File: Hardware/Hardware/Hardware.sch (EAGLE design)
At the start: 9 parts, among them J1 1x10 HEADER "A", J2 1x10 HEADER "B", U1 MAX3232

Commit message: Merged the circuit diagrams
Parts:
- added C11: 1uF, rcl:C-EU025-024X044
- added IC1: 74FST3257DR2G, 74FST3257DR2G:74FST3257DR2G
- added J6: 22-27-2051-05, con-molex:22-27-2051-05
- added Q1, Q2: 200mA/40V, SparkFun-DiscreteSemi:TRANS_NPN-2N3904
- added R1, R2: (no value), rcl:R-EU_0207/7
- added R3, R6: 1K, rcl:R-EU_0207/7
- added R4, R5: 4.7K, rcl:R-EU_0207/7
- added U2: L86-M33, L86-M33:L86-M33
- added U4: 74HC4051D,652, 74HC4051D_652:74HC4051D,652
- U1: device SparkFun-IC-Comms:MAX2323TSSOP -> SparkFun-IC-Comms:MAX2323SOIC16
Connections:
- removed net N$9 (its old number): J1.UART_TX, U1.T1IN
- new net +3V3: C5.2, IC1.VCC, J1.3V3, Q1.C, R3.2, U1.VCC, U2.RESET, U2.VCC, U2.V_BCKP, U4.VCC
- new net N$10: IC1.2B2, U2.RXD1
- new net N$11: IC1.1B1, U1.R1OUT
- new net N$17: IC1.2B1, U1.T1IN
- new net N$18: IC1.S, J1.GPIO_I_A2
- new net N$19: IC1.!OE, J1.SPI_CLK
- new net N$20: J6-1.S, U4.Y0
- new net N$22: J6-2.S, U4.Y1
- new net N$23: J6-3.S, U4.Y2
- new net N$24: J6-4.S, U4.Y3
- new net N$25: R2.2, U4.Z
- new net N$3: IC1.1A, J1.UART_RX
- new net N$47: J1.AIN_A1, R1.2, R2.1
- new net N$49: J2.SPI_CS_D/GPIO_I_B3, U4.S0
- new net N$50: J2.SPI_CS_O/GPIO_I_B4, U4.S1
- new net N$51: J2.GPIO_I_B5, U4.S2
- new net N$52: C11.2, R4.1, R5.1
- new net N$53: C11.1, J2.PWM_B1/GPIO_I_B1
- new net N$54: Q2.B, R5.2, R6.1
- new net N$55: Q1.B, R3.1, R4.2
- new net N$57: Q1.E, Q2.C
- net GND: now also IC1.GND, J2.GND, J6-5.S, Q2.E, R1.1, R6.2, U2.GND, U4.GND, U4.VEE, U4.~E
- net N$5: now also IC1.2A, J1.UART_TX; no longer C5.2, J1.3V3, U1.VCC
- net N$8: now also IC1.1B2, U2.TXD1; no longer J1.UART_RX, U1.R1OUT
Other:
- moved on the sheet: C1, C2, C3, C4, C5, J1, J2, J3

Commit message: Merged and tidied up the circuit, did my part of PCB
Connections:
- net N$10: now also IC1.2B1; no longer IC1.2B2
- net N$11: now also IC1.1B2; no longer IC1.1B1
- net N$17: now also IC1.2B2; no longer IC1.2B1
- net N$18: now also J1.SPI_CLK; no longer J1.GPIO_I_A2
- net N$19: now also J1.GPIO_I_A2; no longer J1.SPI_CLK
- net N$20: now also J6-3.S; no longer J6-1.S
- net N$23: now also J6-1.S; no longer J6-3.S
- net N$8: now also IC1.1B1; no longer IC1.1B2
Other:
- moved on the sheet: J6-1, J6-3
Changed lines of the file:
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@@
 <attribute name="VALUE" x="114.046" y="135.89" size="1.778" layer="96" align="center-left"/>
 </instance>
-<instance part="J6" gate="-1" x="142.24" y="93.98" smashed="yes">
-<attribute name="NAME" x="144.78" y="93.218" size="1.524" layer="95"/>
+<instance part="J6" gate="-1" x="142.24" y="88.9" smashed="yes">
+<attribute name="NAME" x="144.78" y="88.138" size="1.524" layer="95"/>
 </instance>
 <instance part="J6" gate="-2" x="142.24" y="91.44" smashed="yes">
 <attribute name="NAME" x="144.78" y="90.678" size="1.524" layer="95"/>
 </instance>
-<instance part="J6" gate="-3" x="142.24" y="88.9" smashed="yes">
-<attribute name="NAME" x="144.78" y="88.138" size="1.524" layer="95"/>
+<instance part="J6" gate="-3" x="142.24" y="93.98" smashed="yes">
+<attribute name="NAME" x="144.78" y="93.218" size="1.524" layer="95"/>
 </instance>
 <instance part="J6" gate="-4" x="142.24" y="86.36" smashed="yes">
@@
 <net name="N$8" class="0">
 <segment>
-<pinref part="IC1" gate="G$1" pin="1B2"/>
-<wire x1="109.22" y1="152.4" x2="106.68" y2="152.4" width="0.1524" layer="91"/>
-<wire x1="106.68" y1="152.4" x2="106.68" y2="165.1" width="0.1524" layer="91"/>
+<wire x1="106.68" y1="154.94" x2="106.68" y2="165.1" width="0.1524" layer="91"/>
 <wire x1="106.68" y1="165.1" x2="152.4" y2="165.1" width="0.1524" layer="91"/>
 <wire x1="152.4" y1="165.1" x2="152.4" y2="147.32" width="0.1524" layer="91"/>
@@
 <pinref part="U2" gate="G$1" pin="TXD1"/>
 <wire x1="208.28" y1="162.56" x2="200.66" y2="162.56" width="0.1524" layer="91"/>
+<pinref part="IC1" gate="G$1" pin="1B1"/>
+<wire x1="109.22" y1="154.94" x2="106.68" y2="154.94" width="0.1524" layer="91"/>
 </segment>
 </net>
@@
 <wire x1="154.94" y1="162.56" x2="154.94" y2="167.64" width="0.1524" layer="91"/>
 <wire x1="154.94" y1="167.64" x2="104.14" y2="167.64" width="0.1524" layer="91"/>
-<wire x1="104.14" y1="167.64" x2="104.14" y2="144.78" width="0.1524" layer="91"/>
-<pinref part="IC1" gate="G$1" pin="2B2"/>
-<wire x1="104.14" y1="144.78" x2="109.22" y2="144.78" width="0.1524" layer="91"/>
+<wire x1="104.14" y1="167.64" x2="104.14" y2="147.32" width="0.1524" layer="91"/>
+<pinref part="IC1" gate="G$1" pin="2B1"/>
+<wire x1="109.22" y1="147.32" x2="104.14" y2="147.32" width="0.1524" layer="91"/>
 </segment>
 </net>
@@
 <pinref part="U1" gate="G$1" pin="R1OUT"/>
 <wire x1="165.1" y1="109.22" x2="96.52" y2="109.22" width="0.1524" layer="91"/>
-<wire x1="96.52" y1="109.22" x2="96.52" y2="154.94" width="0.1524" layer="91"/>
-<pinref part="IC1" gate="G$1" pin="1B1"/>
-<wire x1="96.52" y1="154.94" x2="109.22" y2="154.94" width="0.1524" layer="91"/>
+<wire x1="96.52" y1="109.22" x2="96.52" y2="152.4" width="0.1524" layer="91"/>
+<pinref part="IC1" gate="G$1" pin="1B2"/>
+<wire x1="109.22" y1="152.4" x2="96.52" y2="152.4" width="0.1524" layer="91"/>
 </segment>
 </net>
@@
 <pinref part="U1" gate="G$1" pin="T1IN"/>
 <wire x1="165.1" y1="114.3" x2="101.6" y2="114.3" width="0.1524" layer="91"/>
-<wire x1="101.6" y1="114.3" x2="101.6" y2="147.32" width="0.1524" layer="91"/>
-<pinref part="IC1" gate="G$1" pin="2B1"/>
-<wire x1="101.6" y1="147.32" x2="109.22" y2="147.32" width="0.1524" layer="91"/>
+<wire x1="101.6" y1="114.3" x2="101.6" y2="144.78" width="0.1524" layer="91"/>
+<pinref part="IC1" gate="G$1" pin="2B2"/>
+<wire x1="109.22" y1="144.78" x2="101.6" y2="144.78" width="0.1524" layer="91"/>
 </segment>
 </net>
@@
 <pinref part="IC1" gate="G$1" pin="S"/>
 <wire x1="109.22" y1="157.48" x2="109.22" y2="162.56" width="0.1524" layer="91"/>
-<wire x1="109.22" y1="162.56" x2="147.32" y2="162.56" width="0.1524" layer="91"/>
-<wire x1="147.32" y1="162.56" x2="147.32" y2="132.08" width="0.1524" layer="91"/>
-<pinref part="J1" gate="G$1" pin="GPIO_I_A2"/>
-<wire x1="55.88" y1="132.08" x2="147.32" y2="132.08" width="0.1524" layer="91"/>
+<wire x1="109.22" y1="162.56" x2="142.24" y2="162.56" width="0.1524" layer="91"/>
+<wire x1="142.24" y1="162.56" x2="142.24" y2="134.62" width="0.1524" layer="91"/>
+<wire x1="142.24" y1="134.62" x2="55.88" y2="134.62" width="0.1524" layer="91"/>
+<pinref part="J1" gate="G$1" pin="SPI_CLK"/>
 </segment>
 </net>
@@
 <pinref part="IC1" gate="G$1" pin="!OE"/>
 <wire x1="134.62" y1="154.94" x2="144.78" y2="154.94" width="0.1524" layer="91"/>
-<wire x1="144.78" y1="154.94" x2="144.78" y2="134.62" width="0.1524" layer="91"/>
-<wire x1="144.78" y1="134.62" x2="55.88" y2="134.62" width="0.1524" layer="91"/>
-<pinref part="J1" gate="G$1" pin="SPI_CLK"/>
+<wire x1="144.78" y1="154.94" x2="144.78" y2="132.08" width="0.1524" layer="91"/>
+<pinref part="J1" gate="G$1" pin="GPIO_I_A2"/>
+<wire x1="144.78" y1="132.08" x2="55.88" y2="132.08" width="0.1524" layer="91"/>
 </segment>
 </net>
@@
 </segment>
 </net>
-<net name="N$20" class="0">
-<segment>
-<pinref part="U4" gate="A" pin="Y0"/>
-<pinref part="J6" gate="-1" pin="S"/>
-<wire x1="134.62" y1="93.98" x2="139.7" y2="93.98" width="0.1524" layer="91"/>
-</segment>
-</net>
 <net name="N$22" class="0">
 <segment>
@@
 <pinref part="J6" gate="-2" pin="S"/>
 <wire x1="134.62" y1="91.44" x2="139.7" y2="91.44" width="0.1524" layer="91"/>
-</segment>
-</net>
-<net name="N$23" class="0">
-<segment>
-<pinref part="J6" gate="-3" pin="S"/>
-<pinref part="U4" gate="A" pin="Y2"/>
-<wire x1="139.7" y1="88.9" x2="134.62" y2="88.9" width="0.1524" layer="91"/>
 </segment>
 </net>
@@
 </segment>
 </net>
+<net name="N$20" class="0">
+<segment>
+<pinref part="U4" gate="A" pin="Y0"/>
+<pinref part="J6" gate="-3" pin="S"/>
+<wire x1="139.7" y1="93.98" x2="134.62" y2="93.98" width="0.1524" layer="91"/>
+</segment>
+</net>
+<net name="N$23" class="0">
+<segment>
+<pinref part="U4" gate="A" pin="Y2"/>
+<pinref part="J6" gate="-1" pin="S"/>
+<wire x1="139.7" y1="88.9" x2="134.62" y2="88.9" width="0.1524" layer="91"/>
+</segment>
+</net>

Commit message: Changes in brd
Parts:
- added J4: 22-27-2021-02, con-molex:22-27-2021-02
- R3, R4, R5, R6: device rcl:R-EU_0207/7 -> rcl:R-EU_0207/2V
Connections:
- net N$53: now also J4-1.S
- net N$57: now also J4-2.S

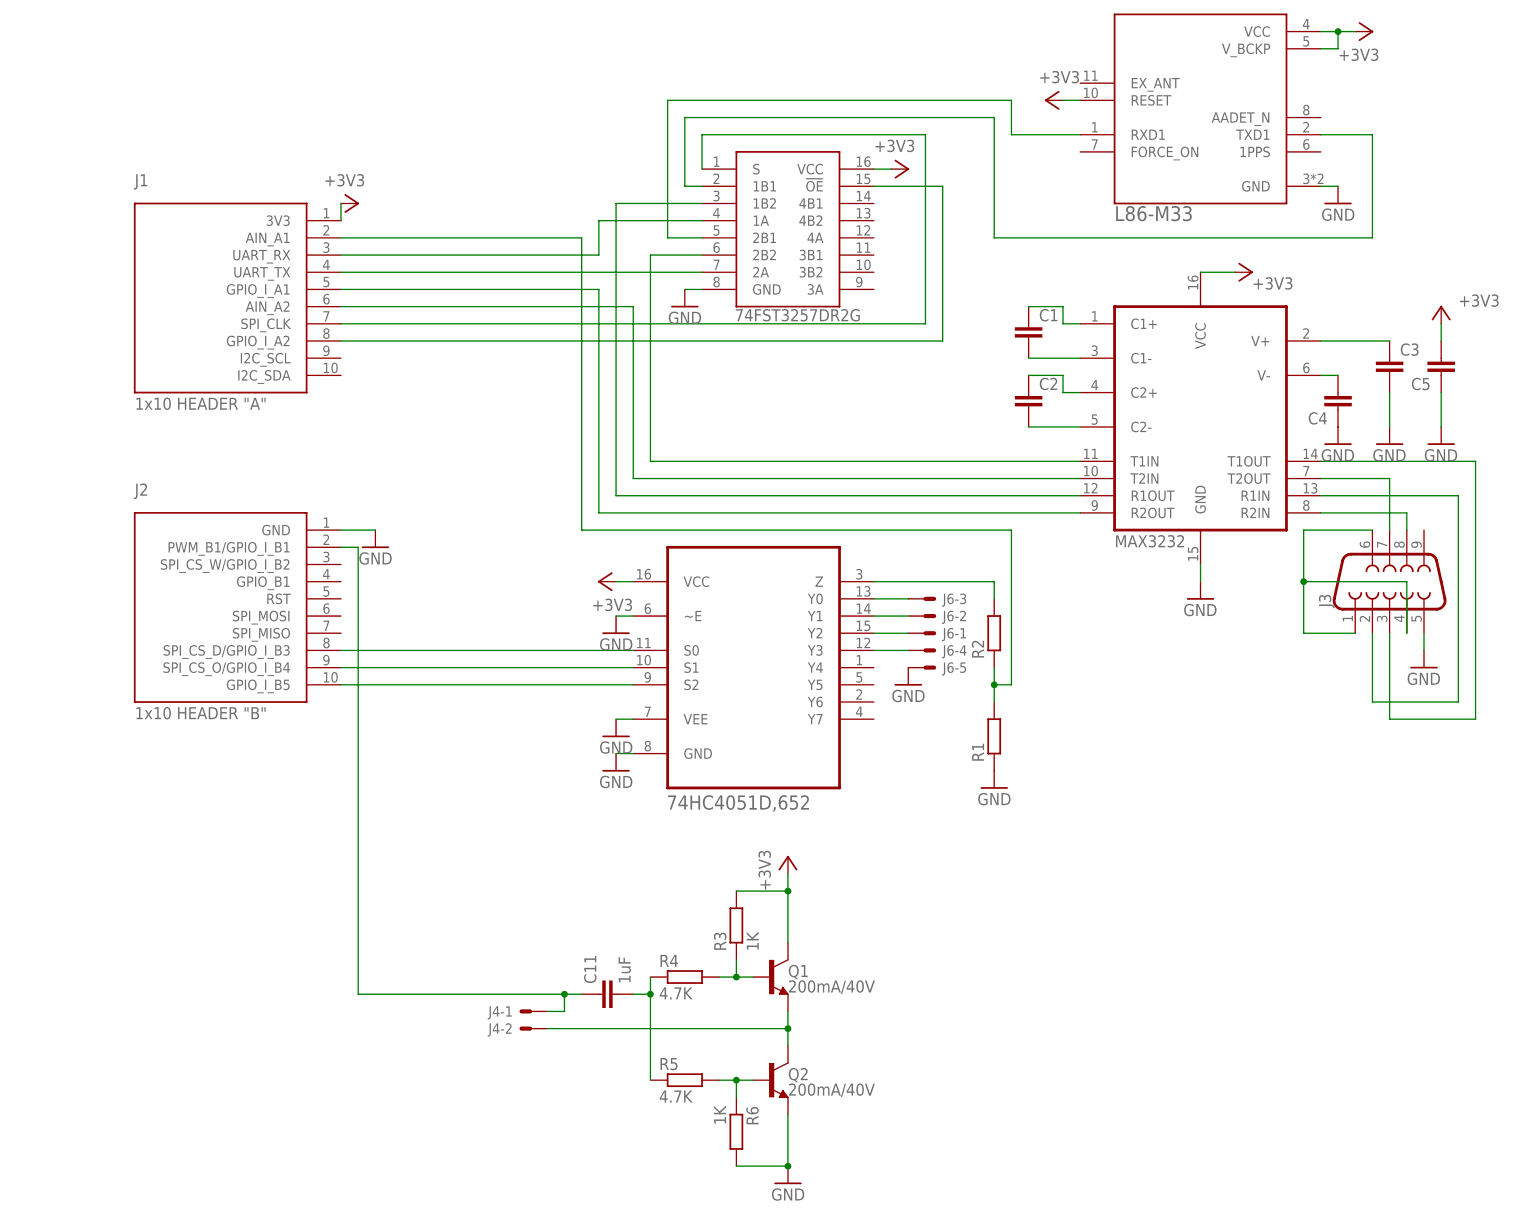
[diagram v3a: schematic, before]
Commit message: Added UART MUX support
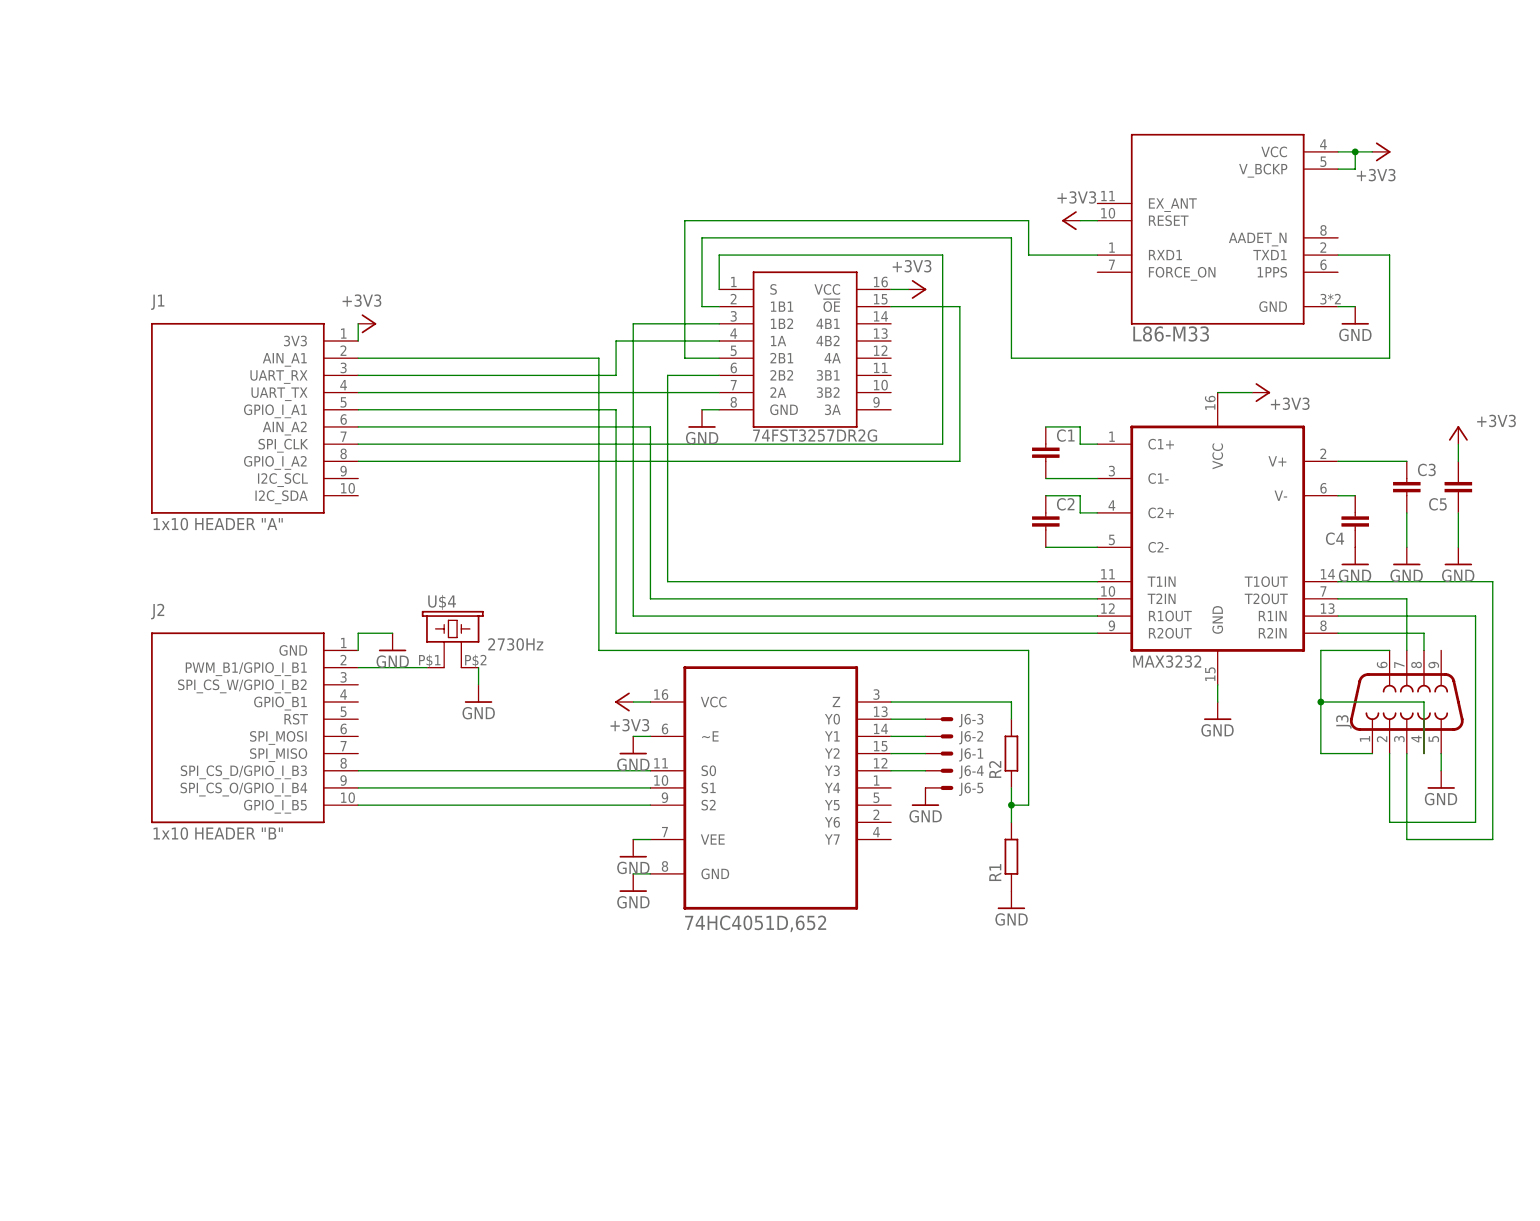
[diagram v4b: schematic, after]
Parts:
- removed C11: 1uF, rcl:C-EU025-024X044
- removed J4: 22-27-2021-02, con-molex:22-27-2021-02
- removed Q1, Q2: 200mA/40V, SparkFun-DiscreteSemi:TRANS_NPN-2N3904
- removed R3, R6: 1K, rcl:R-EU_0207/2V
- removed R4, R5: 4.7K, rcl:R-EU_0207/2V
- added U$4: KCVG084B16, KCVG084B16:KCVG084B16
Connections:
- removed net N$52: C11.2, R4.1, R5.1
- removed net N$53: C11.1, J2.PWM_B1/GPIO_I_B1, J4-1.S
- removed net N$54: Q2.B, R5.2, R6.1
- removed net N$55: Q1.B, R3.1, R4.2
- removed net N$57: J4-2.S, Q1.E, Q2.C
- new net N$31: J2.PWM_B1/GPIO_I_B1, U$4.1
- net +3V3: no longer Q1.C, R3.2
- net GND: now also U$4.2; no longer Q2.E, R6.2
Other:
- moved on the sheet: C1, C2, C3, C4, C5, J1, J2, J3, J6-1, J6-2, J6-3, J6-4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
